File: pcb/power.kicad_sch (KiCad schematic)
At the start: 5 parts, among them J1 CONN_USBC_RCPT_USB2.0_USB4085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

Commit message: Added LSE crystal and started configuring MCU Pinout"
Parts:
- gave numbers to parts that had none: 2
- renumbered C9 to C17, R9 to R12
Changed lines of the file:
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@@
   (symbol (lib_id "arjun_symbols:RES_5K11_1P_1{slash}10W_0603") (at 71.12 86.36 0) (unit 1)
     (in_bom yes) (on_board yes)
-    (property "Reference" "R?" (id 0) (at 67.945 90.17 90)
+    (property "Reference" "R10" (id 0) (at 67.945 90.17 90)
       (effects (font (size 1.27 1.27)) (justify top))
     )
@@
   (symbol (lib_id "power:GND") (at 76.2 99.06 0) (unit 1)
     (in_bom yes) (on_board yes)
-    (property "Reference" "#PWR?" (id 0) (at 76.2 105.41 0)
+    (property "Reference" "#PWR027" (id 0) (at 76.2 105.41 0)
       (effects (font (size 1.27 1.27)) hide)
     )
@@
   (symbol (lib_id "arjun_symbols:CAP_CER_4700p_250V_X7R_0805") (at 33.02 152.4 90) (unit 1)
     (in_bom no) (on_board yes)
-    (property "Reference" "C9" (id 0) (at 38.1 148.59 90)
+    (property "Reference" "C17" (id 0) (at 38.1 148.59 90)
       (effects (font (size 1.27 1.27)) (justify left))
     )
@@
   (symbol (lib_id "arjun_symbols:RES_0R_1{slash}8W_0805") (at 40.64 142.24 270) (unit 1)
     (in_bom yes) (on_board yes)
-    (property "Reference" "R9" (id 0) (at 36.83 139.065 90)
+    (property "Reference" "R12" (id 0) (at 36.83 139.065 90)
       (effects (font (size 1.27 1.27)) (justify top))
     )
@@
   (symbol (lib_id "power:GND") (at 25.4 154.94 0) (unit 1)
     (in_bom yes) (on_board yes)
-    (property "Reference" "#PWR019" (id 0) (at 25.4 161.29 0)
+    (property "Reference" "#PWR030" (id 0) (at 25.4 161.29 0)
       (effects (font (size 1.27 1.27)) hide)
     )
@@
   (symbol (lib_id "power:GND") (at 55.88 119.38 0) (unit 1)
     (in_bom yes) (on_board yes)
-    (property "Reference" "#PWR023" (id 0) (at 55.88 125.73 0)
+    (property "Reference" "#PWR028" (id 0) (at 55.88 125.73 0)
       (effects (font (size 1.27 1.27)) hide)
     )
@@
   (symbol (lib_id "arjun_symbols:RES_5K11_1P_1{slash}10W_0603") (at 81.28 86.36 0) (unit 1)
     (in_bom yes) (on_board yes)
-    (property "Reference" "R?" (id 0) (at 78.105 90.17 90)
+    (property "Reference" "R11" (id 0) (at 78.105 90.17 90)
       (effects (font (size 1.27 1.27)) (justify top))
     )
@@
   (symbol (lib_id "arjun_symbols:CH_GND") (at 48.26 154.94 0) (unit 1)
     (in_bom yes) (on_board yes)
-    (property "Reference" "#PWR020" (id 0) (at 48.26 160.02 0)
+    (property "Reference" "#PWR031" (id 0) (at 48.26 160.02 0)
       (effects (font (size 1.27 1.27)) hide)
     )
@@
   (symbol (lib_id "arjun_symbols:CH_GND") (at 50.8 132.08 0) (unit 1)
     (in_bom yes) (on_board yes)
-    (property "Reference" "#PWR022" (id 0) (at 50.8 137.16 0)
+    (property "Reference" "#PWR029" (id 0) (at 50.8 137.16 0)
       (effects (font (size 1.27 1.27)) hide)
     )
@@
   (symbol (lib_id "power:+5V") (at 50.8 66.04 0) (unit 1)
     (in_bom yes) (on_board yes)
-    (property "Reference" "#PWR021" (id 0) (at 50.8 69.85 0)
-      (effects (font (size 1.27 1.27)) hide)
-    )
+    (property "Reference" "#PWR026" (id 0) (at 50.8 69.85 0)
+      (effects (font (size 1.27 1.27)) hide)
+    )

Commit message: Added 8MHz Oscillator and mapped most of the MCU pins"
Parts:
- renumbered C17 to C19, R10 to R12, R11 to R13, R12 to R14
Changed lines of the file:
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@@
   (symbol (lib_id "arjun_symbols:RES_5K11_1P_1{slash}10W_0603") (at 71.12 86.36 0) (unit 1)
     (in_bom yes) (on_board yes)
-    (property "Reference" "R10" (id 0) (at 67.945 90.17 90)
+    (property "Reference" "R12" (id 0) (at 67.945 90.17 90)
       (effects (font (size 1.27 1.27)) (justify top))
     )
@@
   (symbol (lib_id "power:GND") (at 76.2 99.06 0) (unit 1)
     (in_bom yes) (on_board yes)
-    (property "Reference" "#PWR027" (id 0) (at 76.2 105.41 0)
+    (property "Reference" "#PWR030" (id 0) (at 76.2 105.41 0)
       (effects (font (size 1.27 1.27)) hide)
     )
@@
   (symbol (lib_id "arjun_symbols:CAP_CER_4700p_250V_X7R_0805") (at 33.02 152.4 90) (unit 1)
     (in_bom no) (on_board yes)
-    (property "Reference" "C17" (id 0) (at 38.1 148.59 90)
+    (property "Reference" "C19" (id 0) (at 38.1 148.59 90)
       (effects (font (size 1.27 1.27)) (justify left))
     )
@@
   (symbol (lib_id "arjun_symbols:RES_0R_1{slash}8W_0805") (at 40.64 142.24 270) (unit 1)
     (in_bom yes) (on_board yes)
-    (property "Reference" "R12" (id 0) (at 36.83 139.065 90)
+    (property "Reference" "R14" (id 0) (at 36.83 139.065 90)
       (effects (font (size 1.27 1.27)) (justify top))
     )
@@
   (symbol (lib_id "power:GND") (at 25.4 154.94 0) (unit 1)
     (in_bom yes) (on_board yes)
-    (property "Reference" "#PWR030" (id 0) (at 25.4 161.29 0)
+    (property "Reference" "#PWR033" (id 0) (at 25.4 161.29 0)
       (effects (font (size 1.27 1.27)) hide)
     )
@@
   (symbol (lib_id "power:GND") (at 55.88 119.38 0) (unit 1)
     (in_bom yes) (on_board yes)
-    (property "Reference" "#PWR028" (id 0) (at 55.88 125.73 0)
+    (property "Reference" "#PWR031" (id 0) (at 55.88 125.73 0)
       (effects (font (size 1.27 1.27)) hide)
     )
@@
   (symbol (lib_id "arjun_symbols:RES_5K11_1P_1{slash}10W_0603") (at 81.28 86.36 0) (unit 1)
     (in_bom yes) (on_board yes)
-    (property "Reference" "R11" (id 0) (at 78.105 90.17 90)
+    (property "Reference" "R13" (id 0) (at 78.105 90.17 90)
       (effects (font (size 1.27 1.27)) (justify top))
     )
@@
   (symbol (lib_id "arjun_symbols:CH_GND") (at 48.26 154.94 0) (unit 1)
     (in_bom yes) (on_board yes)
-    (property "Reference" "#PWR031" (id 0) (at 48.26 160.02 0)
+    (property "Reference" "#PWR034" (id 0) (at 48.26 160.02 0)
       (effects (font (size 1.27 1.27)) hide)
     )
@@
   (symbol (lib_id "arjun_symbols:CH_GND") (at 50.8 132.08 0) (unit 1)
     (in_bom yes) (on_board yes)
-    (property "Reference" "#PWR029" (id 0) (at 50.8 137.16 0)
+    (property "Reference" "#PWR032" (id 0) (at 50.8 137.16 0)
       (effects (font (size 1.27 1.27)) hide)
     )
@@
   (symbol (lib_id "power:+5V") (at 50.8 66.04 0) (unit 1)
     (in_bom yes) (on_board yes)
-    (property "Reference" "#PWR026" (id 0) (at 50.8 69.85 0)
-      (effects (font (size 1.27 1.27)) hide)
-    )
+    (property "Reference" "#PWR029" (id 0) (at 50.8 69.85 0)
+      (effects (font (size 1.27 1.27)) hide)
+    )

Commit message: Added Boot mode selection
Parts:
- C19: DNP (none) -> DNP
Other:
- note removed: "DNP"
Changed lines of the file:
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@@
     (effects (font (size 1.27 1.27)) (justify left bottom))
-  )
-  (text "DNP" (at 31.75 152.4 0)
-    (effects (font (size 1.27 1.27) (thickness 0.254) bold) (justify left bottom))
   )
   (label "USB_D_N" (at 50.8 88.9 0)
@@
       (effects (font (size 0.762 0.762)) (justify left))
     )
+    (property "DNP" "DNP" (id 12) (at 33.02 152.4 90))
     (pin "1")
     (pin "2")

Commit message: Changed Boot0 switch to mom. pb, added rotary encoder, and nRST pb
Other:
- note added: "Add ESD protection"
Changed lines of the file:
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@@
+    (effects (font (size 1.27 1.27)) (justify left bottom))
+  )
+  (text "Add ESD protection" (at 71.12 109.22 0)
     (effects (font (size 1.27 1.27)) (justify left bottom))
   )

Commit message: Added MCU pinouts for rotary encoder
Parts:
- removed C19: CAP_CER_4700p_250V_X7R_0805, Capacitor_SMD:C_0805_2012Metric, symbol arjun_symbols:CAP_CER_4700p_250V_X7R_0805
- removed J1: CONN_USBC_RCPT_USB2.0_USB4085-GF-A, arjun_footprints:GCT_USB4085-GF-A_REVA4, symbol arjun_symbols:CONN_USBC_RCPT_USB2.0_USB4085-GF-A
- removed R12, R13: RES_5K11_1P_1/10W_0603, Resistor_SMD:R_0603_1608Metric, symbol arjun_symbols:RES_5K11_1P_1/10W_0603
- removed R14: RES_0R_1/8W_0805, Resistor_SMD:R_0805_2012Metric, symbol arjun_symbols:RES_0R_1/8W_0805
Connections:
- no-connect marks 4 -> 0
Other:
- note removed: "Add ESD protection"
- note removed: "Standard USB2.0 UFP Device"

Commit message: Added IN-3 dots, picked FTDI chip and 3.3V LDO
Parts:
- added U5: REG_3V3_150mA_SOT23_DI_AP2120N-3.3TRG1, arjun_footprints:DIO_SOT-23, symbol arjun_symbols:REG_3V3_150mA_SOT23_DI_AP2120N-3.3TRG1
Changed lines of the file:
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@@
 (kicad_sch (version 20211123) (generator eeschema)
   (paper "A4")
+  (symbol (lib_id "arjun_symbols:REG_3V3_150mA_SOT23_DI_AP2120N-3.3TRG1") (at 60.96 33.02 0) (unit 1)
+    (in_bom yes) (on_board yes)
+    (property "Reference" "U5" (id 0) (at 64.77 29.845 0))
+    (property "Value" "REG_3V3_150mA_SOT23_DI_AP2120N-3.3TRG1" (id 1) (at 91.44 33.02 0)
+      (effects (font (size 1.27 1.27)) (justify left) hide)
+    )
+    (property "Footprint" "arjun_footprints:DIO_SOT-23" (id 2) (at 91.44 30.48 0)
+      (effects (font (size 1.27 1.27) italic) (justify left) hide)
+    )
+    (property "Datasheet" "https://www.diodes.com/assets/Datasheets/AP2127.pdf" (id 3) (at 91.44 45.72 0)
+      (effects (font (size 1.27 1.27)) (justify left) hide)
+    )
+    (property "Manufacturer" "Diodes Incorporated" (id 4) (at 91.44 38.1 0)
+      (effects (font (size 1.27 1.27)) (justify left) hide)
+    )
+    (property "ManufacturerPN" "AP2120N-3.3TRG1" (id 5) (at 69.215 41.91 0)
+      (effects (font (size 1.016 1.016)))
+    )
+    (property "Vendor" "Digi-Key" (id 6) (at 91.44 40.64 0)
+      (effects (font (size 1.27 1.27)) (justify left) hide)
+    )
+    (property "VendorPN" "AP2120N-3.3TRG1DICT-ND" (id 7) (at 91.44 43.18 0)
+      (effects (font (size 1.27 1.27)) (justify left) hide)
+    )
+    (property "Voltage" "3.3V" (id 8) (at 69.85 29.845 0)
+      (effects (font (size 1.27 1.27)) (justify left))
+    )
+    (property "Current" "150mA" (id 9) (at 91.44 53.34 0)
+      (effects (font (size 1.27 1.27)) (justify left) hide)
+    )
+    (property "Vin_max" "6V" (id 10) (at 91.44 48.26 0)
+      (effects (font (size 1.27 1.27)) (justify left) hide)
+    )
+    (pin "1")
+    (pin "2")
+    (pin "3")
+  )
 )

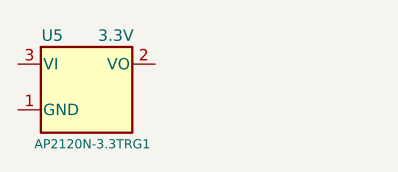
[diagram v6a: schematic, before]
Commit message: 12V boost sim in a good place with calculated values
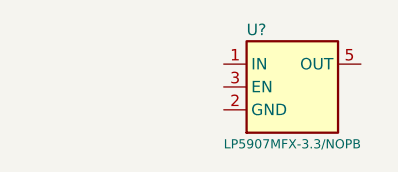
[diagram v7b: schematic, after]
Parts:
- removed U5: REG_3V3_150mA_SOT23_DI_AP2120N-3.3TRG1, arjun_footprints:DIO_SOT-23, symbol arjun_symbols:REG_3V3_150mA_SOT23_DI_AP2120N-3.3TRG1
- added U?: REG_LDO_3V3_250mA_TI_LP5907MFX-3.3, arjun_footprints:SOT-23-5_TI, symbol .arjun:REG_LDO_3V3_250mA_TI_LP5907MFX-3.3
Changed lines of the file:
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@@
 (kicad_sch (version 20211123) (generator eeschema)
   (paper "A4")
-  (symbol (lib_id "arjun_symbols:REG_3V3_150mA_SOT23_DI_AP2120N-3.3TRG1") (at 60.96 33.02 0) (unit 1)
+  (symbol (lib_id ".arjun:REG_LDO_3V3_250mA_TI_LP5907MFX-3.3") (at 83.82 33.02 0) (unit 1)
     (in_bom yes) (on_board yes)
-    (property "Reference" "U5" (id 0) (at 64.77 29.845 0))
-    (property "Value" "REG_3V3_150mA_SOT23_DI_AP2120N-3.3TRG1" (id 1) (at 91.44 33.02 0)
+    (property "Reference" "U?" (id 0) (at 86.36 29.21 0)
+      (effects (font (size 1.27 1.27)) (justify left))
+    )
+    (property "Value" "REG_LDO_3V3_250mA_TI_LP5907MFX-3.3" (id 1) (at 113.03 24.13 0)
       (effects (font (size 1.27 1.27)) (justify left) hide)
     )
-    (property "Footprint" "arjun_footprints:DIO_SOT-23" (id 2) (at 91.44 30.48 0)
-      (effects (font (size 1.27 1.27) italic) (justify left) hide)
-    )
-    (property "Datasheet" "https://www.diodes.com/assets/Datasheets/AP2127.pdf" (id 3) (at 91.44 45.72 0)
+    (property "Footprint" "arjun_footprints:SOT-23-5_TI" (id 2) (at 113.03 21.59 0)
       (effects (font (size 1.27 1.27)) (justify left) hide)
     )
-    (property "Manufacturer" "Diodes Incorporated" (id 4) (at 91.44 38.1 0)
+    (property "Datasheet" "http://www.ti.com/lit/ds/symlink/lp5907.pdf" (id 3) (at 113.03 39.37 0)
       (effects (font (size 1.27 1.27)) (justify left) hide)
     )
-    (property "ManufacturerPN" "AP2120N-3.3TRG1" (id 5) (at 69.215 41.91 0)
+    (property "Manufacturer" "Texas Instruments" (id 4) (at 113.03 36.83 0)
+      (effects (font (size 1.27 1.27)) (justify left) hide)
+    )
+    (property "ManufacturerPN" "LP5907MFX-3.3/NOPB" (id 5) (at 91.44 41.91 0)
       (effects (font (size 1.016 1.016)))
     )
-    (property "Vendor" "Digi-Key" (id 6) (at 91.44 40.64 0)
+    (property "Vendor" "Digi-Key" (id 6) (at 113.03 30.48 0)
       (effects (font (size 1.27 1.27)) (justify left) hide)
     )
-    (property "VendorPN" "AP2120N-3.3TRG1DICT-ND" (id 7) (at 91.44 43.18 0)
-      (effects (font (size 1.27 1.27)) (justify left) hide)
-    )
-    (property "Voltage" "3.3V" (id 8) (at 69.85 29.845 0)
-      (effects (font (size 1.27 1.27)) (justify left))
-    )
-    (property "Current" "150mA" (id 9) (at 91.44 53.34 0)
-      (effects (font (size 1.27 1.27)) (justify left) hide)
-    )
-    (property "Vin_max" "6V" (id 10) (at 91.44 48.26 0)
+    (property "VendorPN" "296-38557-1-ND" (id 7) (at 113.03 33.02 0)
       (effects (font (size 1.27 1.27)) (justify left) hide)
     )
@@
     (pin "2")
     (pin "3")
+    (pin "4")
+    (pin "5")
   )
 )

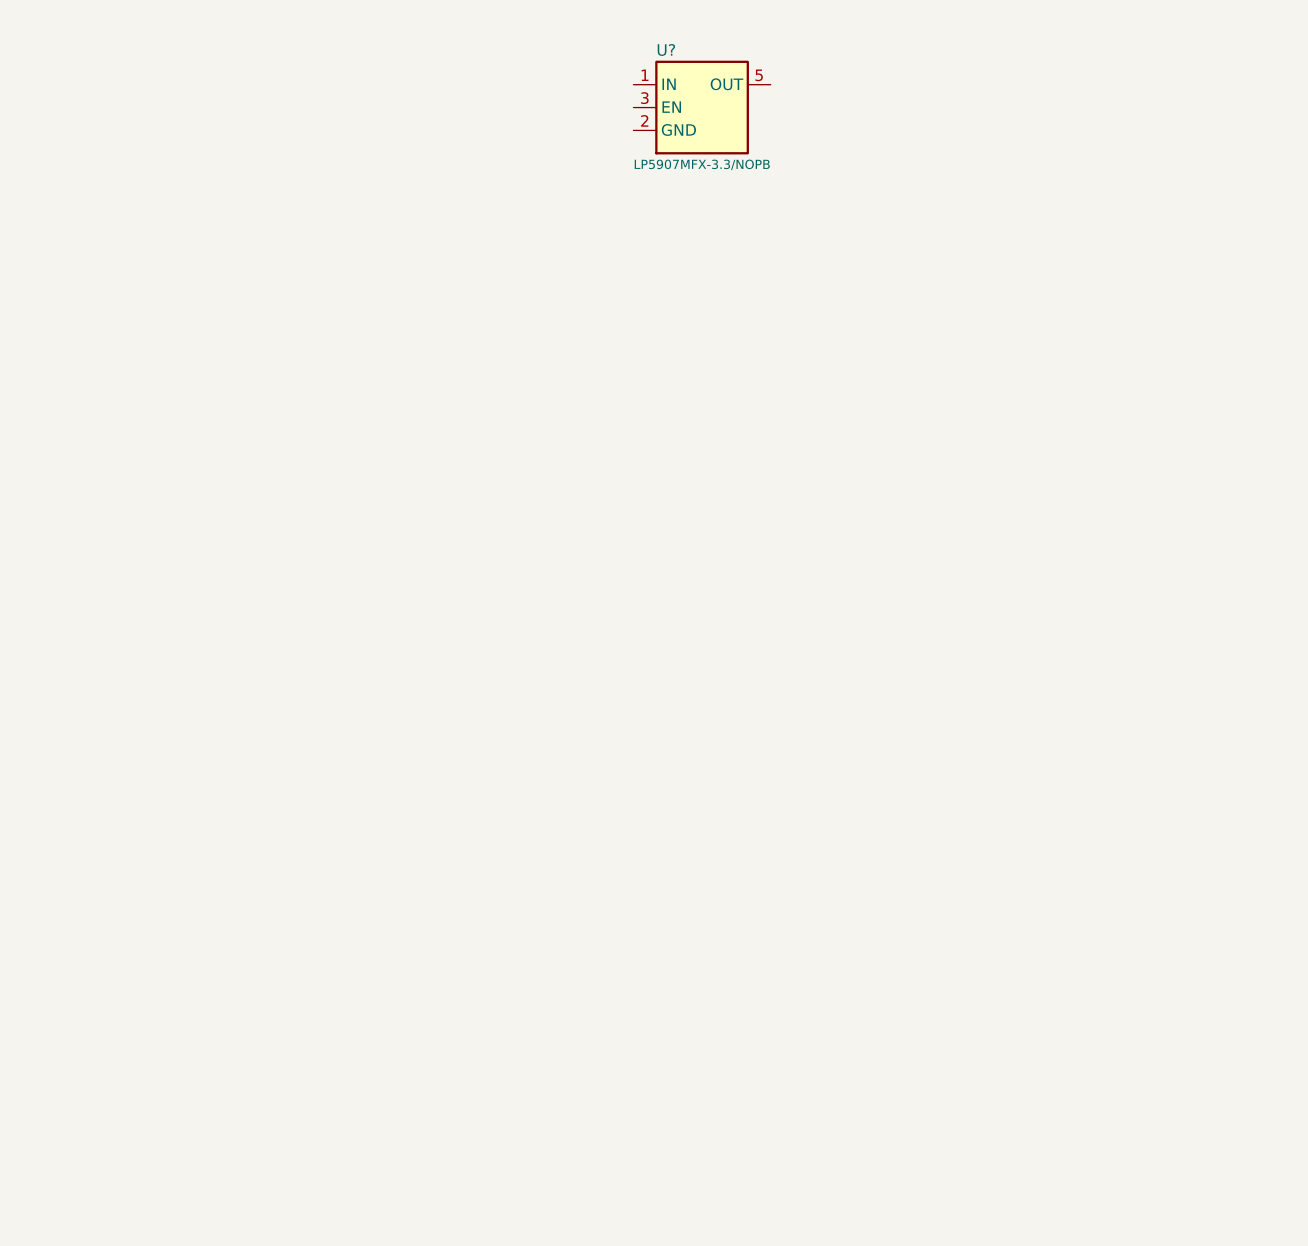
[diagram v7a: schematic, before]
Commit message: Finished 12V boost circuit and updated sim to match
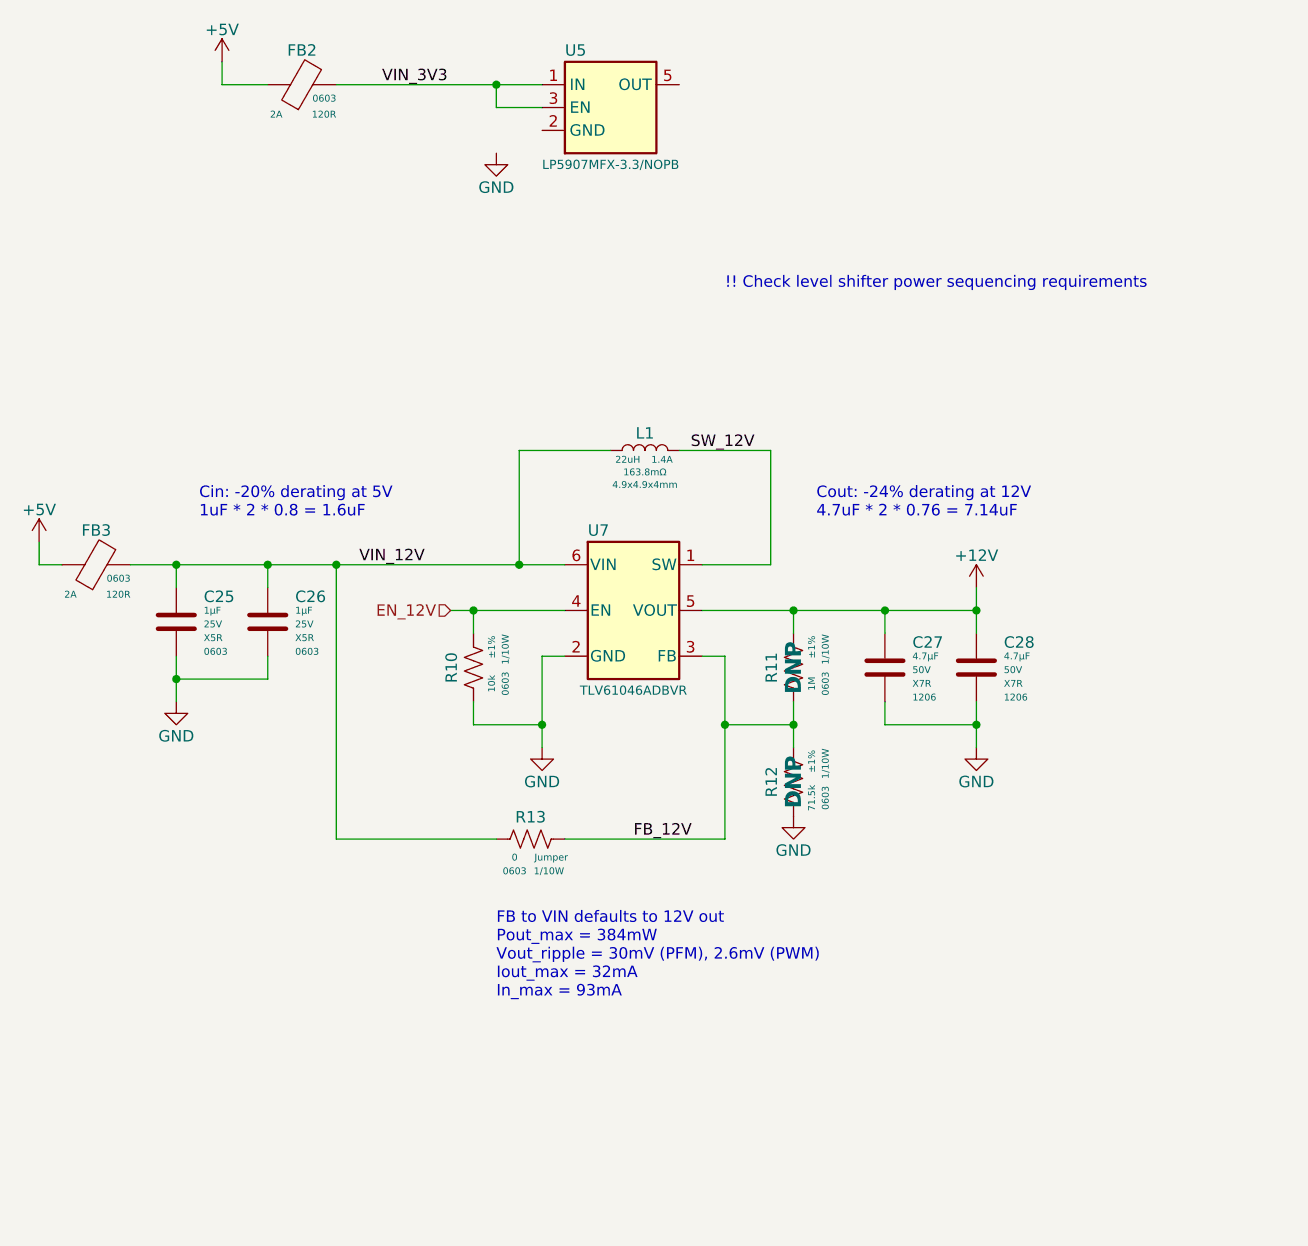
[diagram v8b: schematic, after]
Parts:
- added C25, C26: CAP_CER_1u_25V_X5R_0603, Capacitor_SMD:C_0603_1608Metric, symbol .arjun:CAP_CER_1u_25V_X5R_0603
- added C27, C28: CAP_CER_4u7_50V_X7R_1206, Capacitor_SMD:C_1206_3216Metric, symbol .arjun:CAP_CER_4u7_50V_X7R_1206
- added FB2, FB3: FER_120R_2A_0603, Inductor_SMD:L_0603_1608Metric, symbol .arjun:FER_120R_2A_0603
- added L1: IND_22u_1A4_163m8R_4r9x4r9x4, arjun_footprints:L_Taiyo-Yuden_NR-50xx, symbol .arjun:IND_22u_1A4_163m8R_4r9x4r9x4
- added R10: RES_10K_1P_1/10W_0603, Resistor_SMD:R_0603_1608Metric, symbol .arjun:RES_10K_1P_1/10W_0603
- added R11: RES_1M_1P_1/10W_0603, Resistor_SMD:R_0603_1608Metric, symbol .arjun:RES_1M_1P_1/10W_0603
- added R12: RES_71K5_1P_1/10W_0603, Resistor_SMD:R_0603_1608Metric, symbol .arjun:RES_71K5_1P_1/10W_0603
- added R13: RES_0R_1/10W_0603, Resistor_SMD:R_0603_1608Metric, symbol .arjun:RES_0R_1/10W_0603
- added U7: REG_SW_BOOST_TI_TLV61046ADBV, arjun_footprints:SOT-23-6_TI, symbol .arjun:REG_SW_BOOST_TI_TLV61046ADBV
- gave numbers to parts that had none: 1
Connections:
- net VIN_3V3: now reaches U5.1 (IN)
- net VIN_3V3: now also U5.3 (EN), FB2.2
- new net +12V: C27.1, C28.1, R11.1, U7.5 (VOUT)
- new net +5V: FB2.1, FB3.1
- new net EN_12V: R10.1, U7.4 (EN)
- new net FB_12V: R11.2, R12.1, R13.1, U7.3 (FB)
- new net GND: C25.2, C26.2, C27.2, C28.2, R10.2, R12.2, U7.2 (GND)
- new net SW_12V: L1.2, U7.1 (SW)
- new net VIN_12V: C25.1, C26.1, FB3.2, L1.1, R13.2, U7.6 (VIN)
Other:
- note added: "!! Check level shifter power sequencing requirements"
- note added: "Cin: -20% derating at 5V 1uF * 2 * 0.8 = 1.6uF"
- note added: "Cout: -24% derating at 12V 4.7uF * 2 * 0.76 = 7.14uF"
- note added: "FB to VIN defaults to 12V out Pout_max = 384mW Vout_ripple = 30mV (PFM), 2.6mV (PWM) Iout_max = 32mA In_max = 93mA"
- moved on the sheet: U5
